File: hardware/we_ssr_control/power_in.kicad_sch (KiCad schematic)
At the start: 10 parts, among them Q1 IRF4905PBF

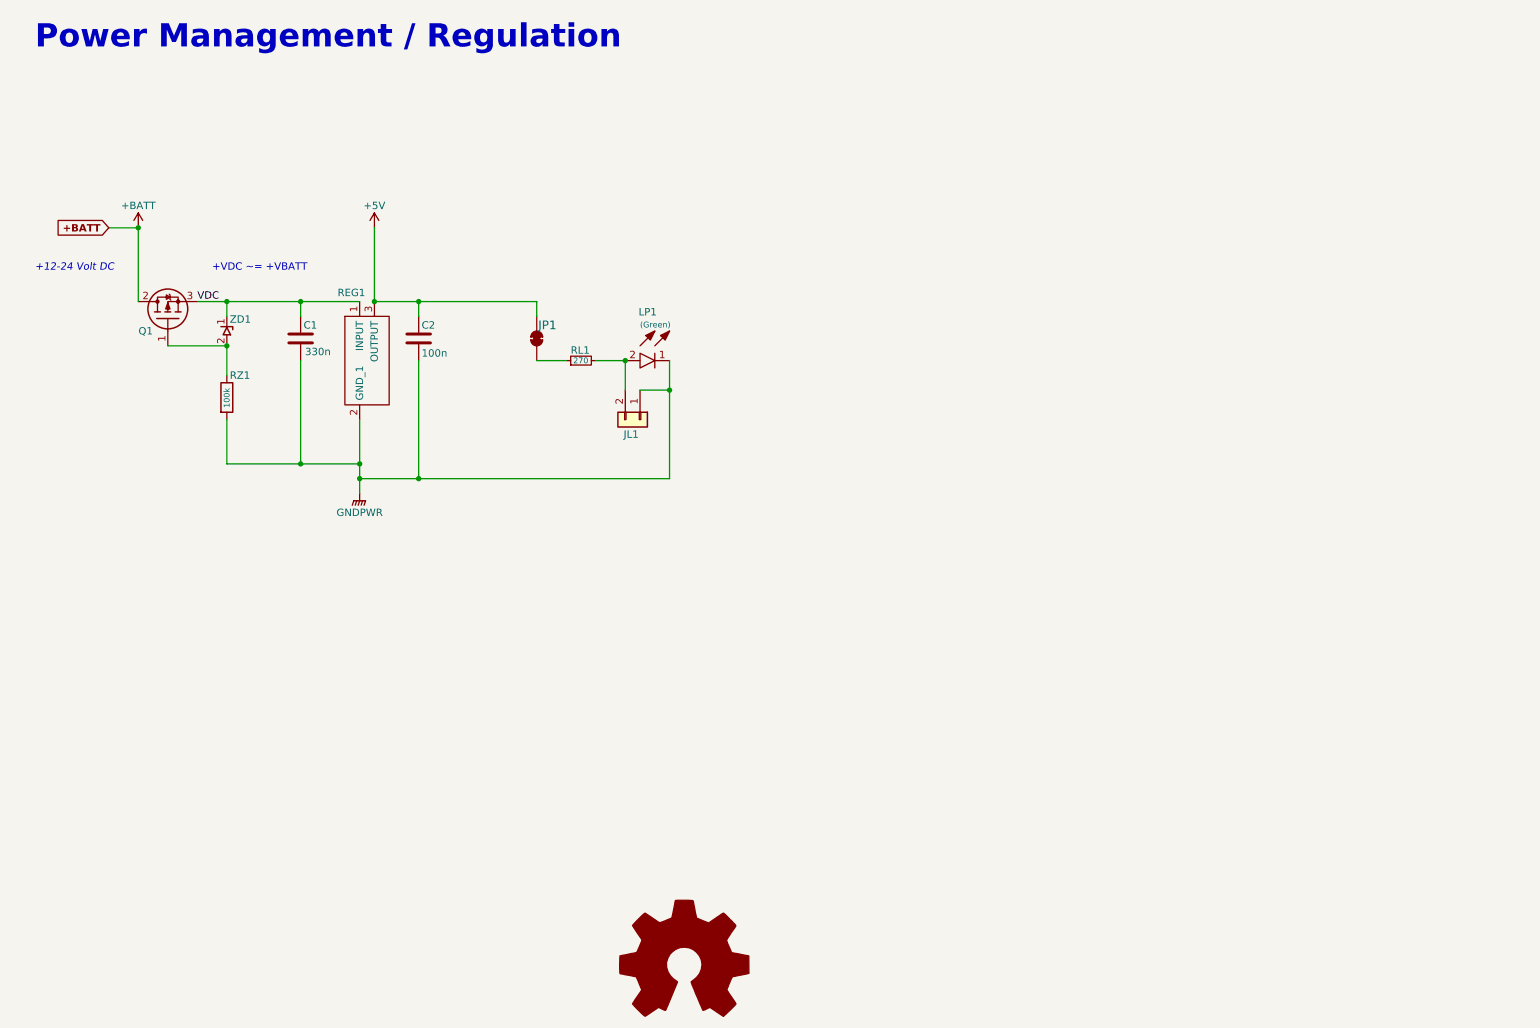
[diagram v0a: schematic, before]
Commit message: Power supply changes plus misc.
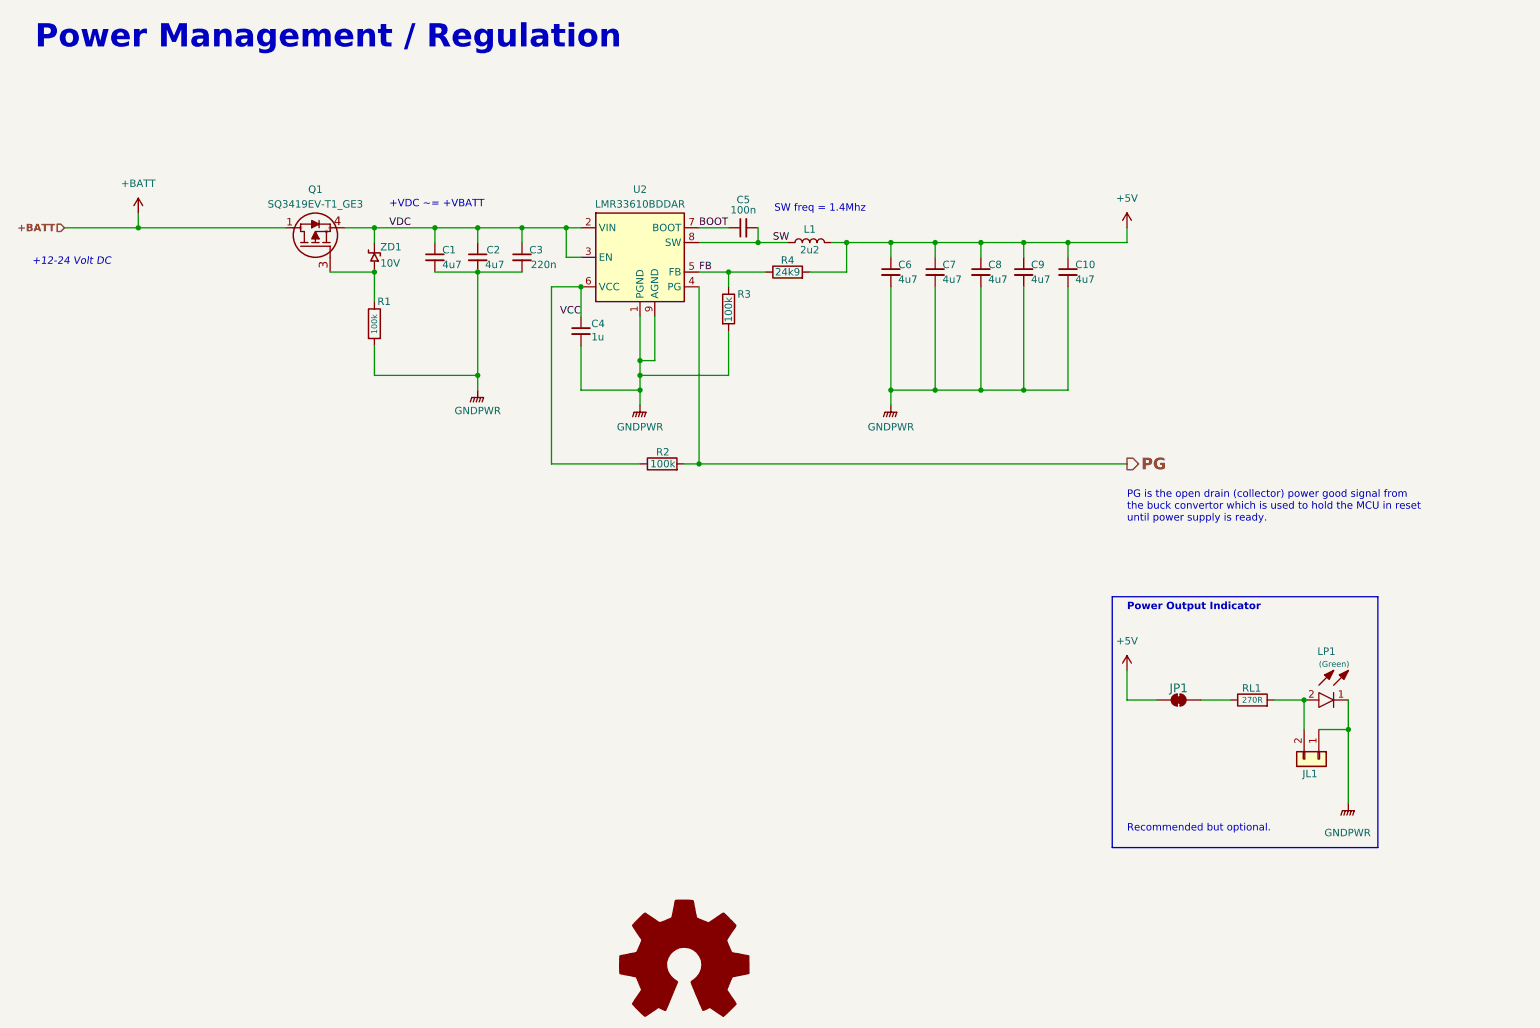
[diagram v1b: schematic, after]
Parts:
- removed C1: 330n, Capacitor_SMD:C_0805_2012Metric, symbol Device:C
- removed C2: 100n, Capacitor_SMD:C_0805_2012Metric, symbol Device:C
- removed Q1: IRF4905PBF, dragon_mobile:TO254P469X1042X1967-3P, symbol dragon_mobile:IRF4905PBF
- removed REG1: LM7805, Package_TO_SOT_SMD:SOT-223, symbol dragon_mobile:LM7805MPX_NOPB
- removed RZ1: 100k, Resistor_SMD:R_0603_1608Metric, symbol Device:R
- removed ZD1: +10v Zener Diode, dragon_mobile:BZD27C10P-M3-08, symbol dragon_mobile:BZD27C10P-M3-08
- added C1, C10, C2, C6, C7, C8, C9: 4u7, Capacitor_SMD:C_0805_2012Metric, symbol Device:C_Small
- added C3: 220n, Capacitor_SMD:C_0603_1608Metric, symbol Device:C_Small
- added C4: 1u, Capacitor_SMD:C_0603_1608Metric, symbol Device:C_Small
- added C5: 100n, Capacitor_SMD:C_0603_1608Metric, symbol Device:C_Small
- added L1: 2u2, Inductor_SMD:L_1008_2520Metric, symbol Device:L
- added Q1: SQ3419EV-T1_GE3, dragon_mobile:SOT95P284X110-6N, symbol dragon_mobile:SQ3419EV-T1_BE3
- added R1, R2, R3: 100k, Resistor_SMD:R_0603_1608Metric, symbol Device:R
- added R4: 24k9, Resistor_SMD:R_0603_1608Metric, symbol Device:R
- added U2: LMR33610BDDAR, Package_SO:Texas_HSOP-8-1EP_3.9x4.9mm_P1.27mm_ThermalVias, symbol Regulator_Switching:LMR33610BDDAR
- added ZD1: 10V, Diode_SMD:D_0805_2012Metric, symbol dragon_mobile:TSZU52C10
- JL1: footprint Connector_PinHeader_1.00mm:PinHeader_1x02_P1.00mm_Vertical -> dragon_mobile:PinHeader_1x02_P1.00mm_Vertical; Characteristics (none) -> Pin Header; 1mm 1x2 Vertical
- LP1: Manufacturer_Name Lite-On -> (none); Manufacturer_Part_Number LTST-C190KGKT -> (none)
- RL1: value 270 -> 270R; symbol Device:R_Small -> Device:R; Height (mm) (none) -> 0.45
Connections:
- net +5V: now also C10.1, C6.1, C7.1, C8.1, C9.1, L1.2, R4.2
- net +BATT: now also Q1.1 (D), Q1.2 (D), Q1.5 (D), Q1.6 (D)
- net GNDPWR: now also C1.2, C10.2, C2.2, C3.2, C4.2, C6.2, C7.2, C8.2, C9.2, R1.2, R3.2, U2.1 (PGND), U2.9 (AGND)
- net VDC: now also C1.1, C2.1, C3.1, Q1.4 (S), U2.2 (VIN), U2.3 (EN), ZD1.1
- new net: Q1.3 (G), R1.1, ZD1.2
- new net BOOT: C5.1, U2.7 (BOOT)
- new net FB: R3.1, R4.1, U2.5 (FB)
- new net PG: R2.2, U2.4 (PG)
- new net SW: C5.2, L1.1, U2.8 (SW)
- new net VCC: C4.1, R2.1, U2.6 (VCC)
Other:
- note added: "PG is the open drain (collector) power good signal from the buck convertor which is used to hold the MCU in reset until power supply is ready."
- note added: "Power Output Indicator"
- note added: "Recommended but optional."
- note added: "SW freq = 1.4Mhz"
- moved on the sheet: JL1, JP1, LP1, RL1
